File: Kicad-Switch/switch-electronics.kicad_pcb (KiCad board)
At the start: 2 copper layers, 99.1 x 99.1 mm, 95 parts, among them M1 CONN_1, P1 CONN_12, Q1 2N3906, Q10 SQD45P03-12-GE3, Q12 SQD45P03-12-GE3, Q13 SQD45P03-12-GE3, Q15 SQD45P03-12-GE3, Q16 SQD45P03-12-GE3, Q18 SQD45P03-12-GE3, Q2 2N3906, Q3 2N3906, Q4 2N3906, Q5 2N3906, Q6 2N3906, Q7 2N3906, Q8 2N3906, Q9 2N3906, U1 74HC04, U2 74LS139, U3 74HC04, U4 74LS139, U7 LM7809CT, U8 LM1084IT-3.3/NOPB

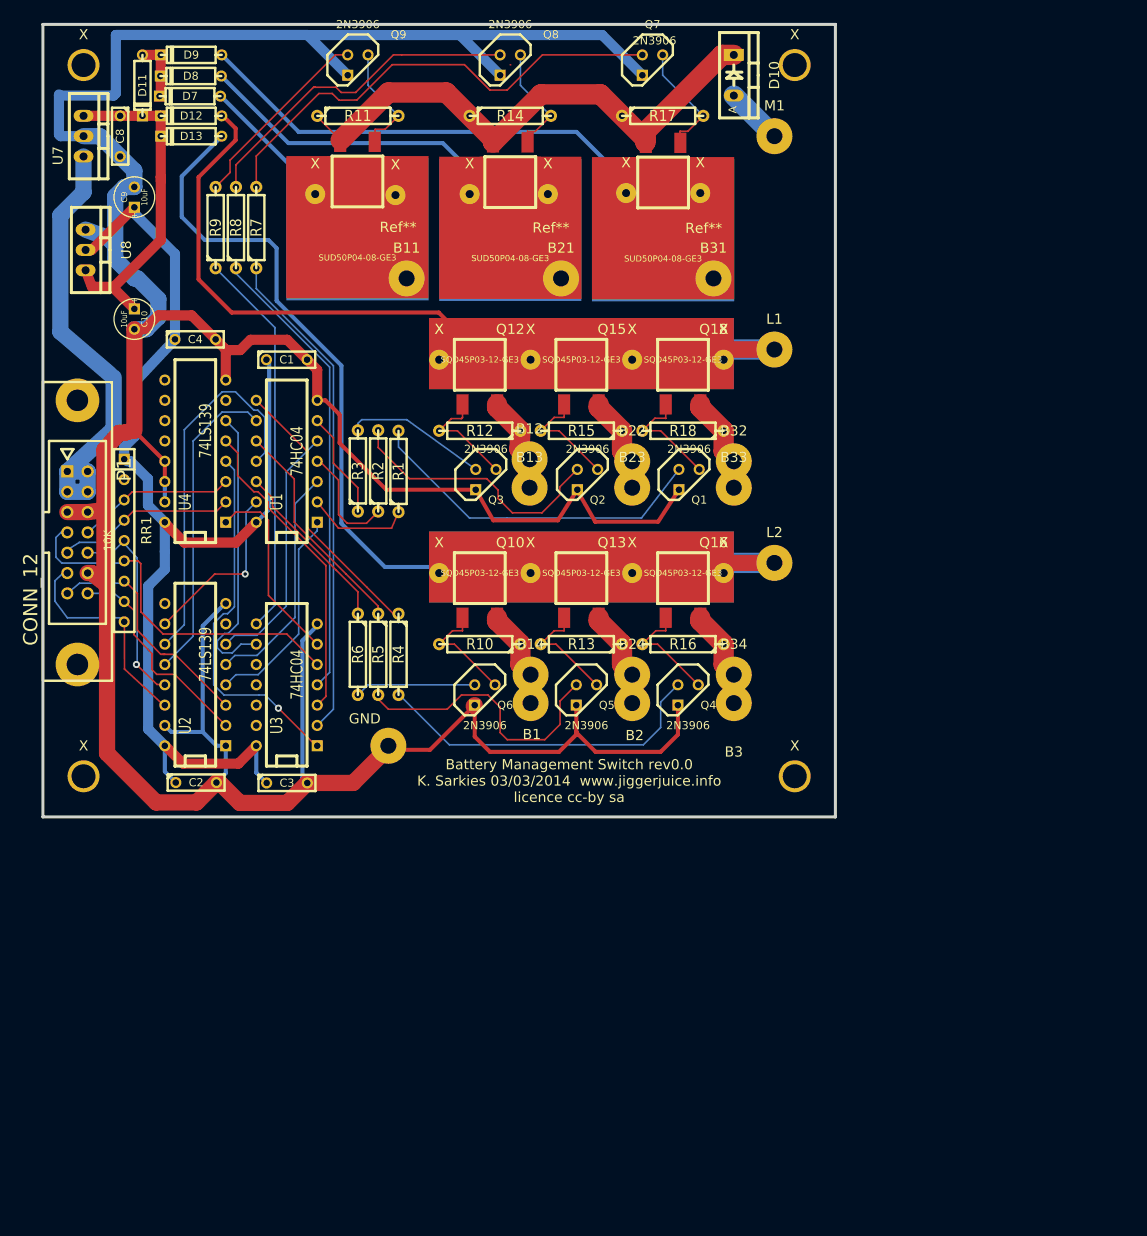
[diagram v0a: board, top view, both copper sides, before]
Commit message: Switch PCB: first Kicad version complete, not yet verified.
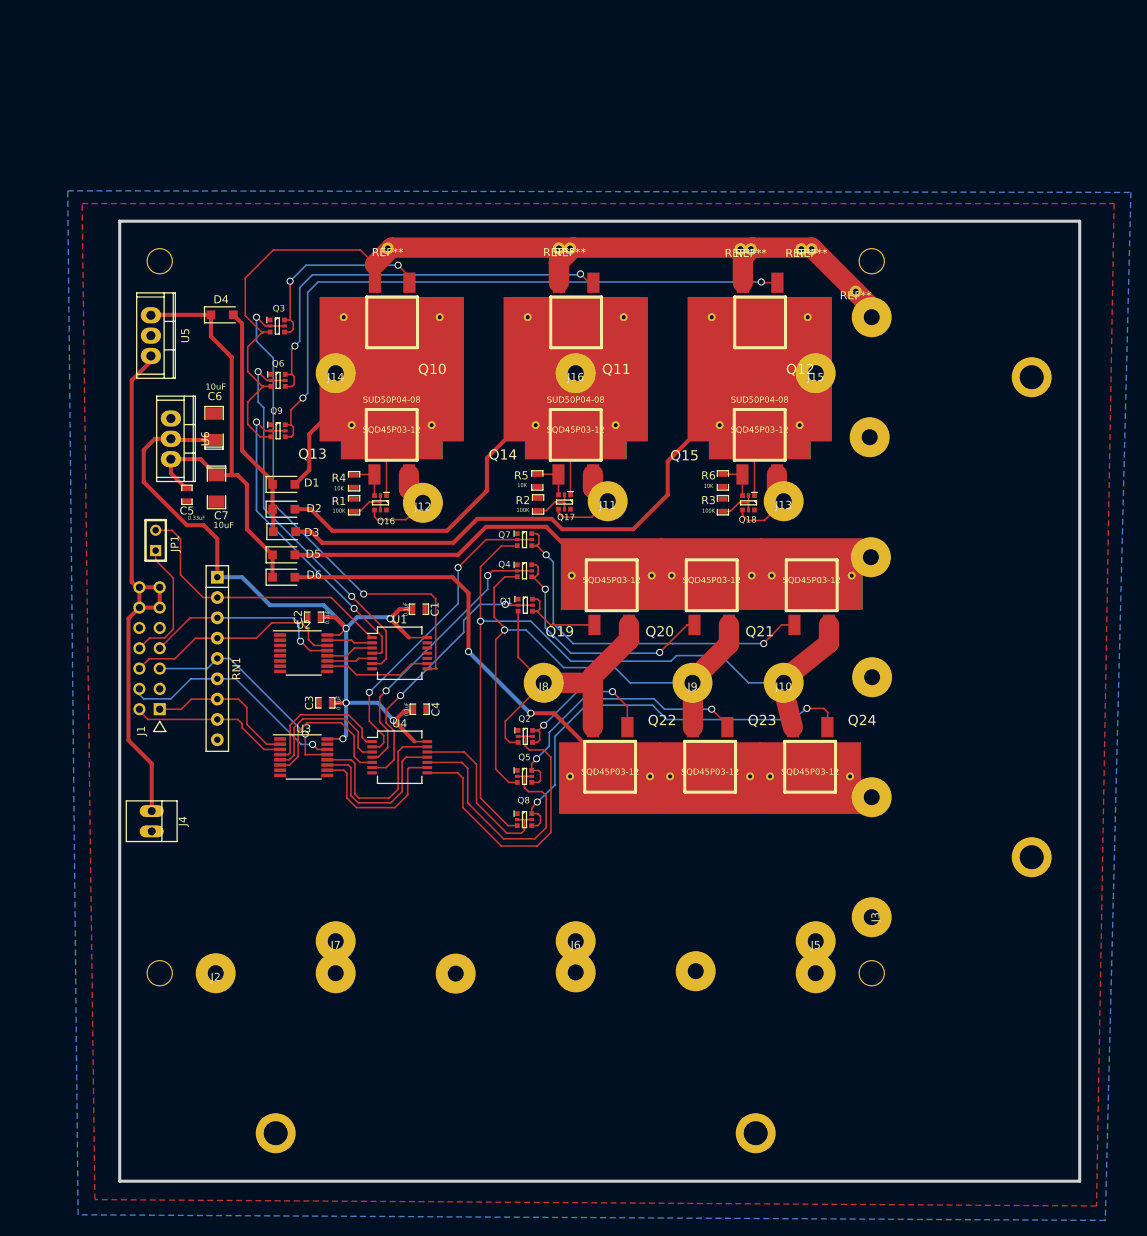
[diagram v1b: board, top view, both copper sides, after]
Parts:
- removed B1, B11, B12, B13, B14, B2, B21, B22, B23, B24, B3, B31, B32, B33, B34, GND, L1, L2, M1: CONN_1, SolderWirePad_single_2mmDrill
- removed C10, C9: 10uF, C1V5
- removed C8: 0.1uF, C2
- removed D10: MBR1645, Diode_TO-220_Vertical
- removed D11, D7, D8, D9: 1N4701, D3
- removed D12, D13: 1N5819, D3
- removed P1: CONN_12, he10-14d
- removed R10, R11, R12, R13, R14, R15, R16, R17, R18: 1K, R4
- removed R7, R8, R9: 10K, R4
- removed RR1: 10K, r_pack8
- removed Ref** (x3): SUD50P04-08-GE3, Fred:TO252-HS
- removed U7: LM7809CT, TO-220_Neutral123_Vertical
- removed U8: LM1084IT-3.3/NOPB, Transistors_TO-220:TO-220_Neutral123_Vertical
- removed X (x4): SolderWirePad_single_2mmDrill, SolderWirePad_single_2mmDrill
- removed X (x14): SolderWirePad_single_1mmDrill, SolderWirePad_single_1mmDrill
- added ?: MountingHole, BMS:Mounting_Hole_3mm, F.Cu at (40.0, 55.0)
- added ?: MountingHole, BMS:Mounting_Hole_3mm, F.Cu at (129.0, 55.0)
- added ?: MountingHole, BMS:Mounting_Hole_3mm, F.Cu at (129.0, 144.0)
- added ?: MountingHole, BMS:Mounting_Hole_3mm, F.Cu at (40.0, 144.0)
- added C5: 0.33uF, BMS:SM0603_Capa, F.Cu at (43.4, 84.2)
- added C6: 10uF, BMS:SM1206POL, F.Cu at (46.8, 75.7)
- added C7: 10uF, BMS:SM1206POL, F.Cu at (47.1, 83.4)
- added D1: 1N4001, BMS:D_SOD-123F, F.Cu at (55.5, 82.9)
- added D2: 1N4001, BMS:D_SOD-123F, F.Cu at (55.5, 86.0)
- added D3: 1N4001, BMS:D_SOD-123F, F.Cu at (55.6, 88.8)
- added D4: 1N4001, BMS:D_SOD-123F, F.Cu at (47.8, 61.7)
- added D5: 2N5819, BMS:D_SOD-123F, F.Cu at (55.5, 91.7)
- added D6: 2N5819, BMS:D_SOD-123F, F.Cu at (55.5, 94.5)
- added J1: Conn_02x07_Odd_Even, BMS:header-14-v, F.Cu at (40.0, 111.0)
- added J10: Conn_01x01, BMS:Pad_Large, F.Cu at (118.0, 107.7)
- added J11: Conn_01x01, BMS:Pad_Large, F.Cu at (96.0, 85.0)
- added J12: Conn_01x01, BMS:Pad_Large, F.Cu at (72.9, 85.2)
- added J13: Conn_01x01, BMS:Pad_Large, F.Cu at (118.0, 85.0)
- added J14: Conn_01x01, BMS:Pad_Large, F.Cu at (62.0, 69.0)
- added J15: Conn_01x01, BMS:Pad_Large, F.Cu at (122.0, 69.0)
- added J16: Conn_01x01, BMS:Pad_Large, F.Cu at (92.0, 69.0)
- added J2: Screw_Terminal_01x06, BMS:Screw_Terminal_Six, F.Cu at (47.0, 144.0)
- added J3: Screw_Terminal_01x06, BMS:Screw_Terminal_Six, F.Cu at (129.0, 137.0)
- added J4: Conn_01x02, BMS:PINHEAD1-2, F.Cu at (39.0, 125.0)
- added J5: Conn_01x01, BMS:Pad_Large, F.Cu at (122.0, 140.0)
- added J6: Conn_01x01, BMS:Pad_Large, F.Cu at (92.0, 140.0)
- added J7: Conn_01x01, BMS:Pad_Large, F.Cu at (62.0, 140.0)
- added J8: Conn_01x01, BMS:Pad_Large, F.Cu at (88.0, 107.7)
- added J9: Conn_01x01, BMS:Pad_Large, F.Cu at (106.6, 107.7)
- added JP1: Jumper_NO_Small, BMS:SIL-2, F.Cu at (39.5, 89.9)
- added Q11: SUD50P04-08, BMS:TO252-HS-Large, F.Cu at (92.0, 52.0)
- added Q14: SQD45P03-12, BMS:TO252-HS-Small, F.Cu at (92.0, 87.5)
- added Q17: BC856BDW1, BMS:SOT-363, F.Cu at (90.6, 85.1)
- added Q19: SQD45P03-12, BMS:TO252-HS-Small, F.Cu at (96.5, 106.3)
- added Q20: SQD45P03-12, BMS:TO252-HS-Small, F.Cu at (109.0, 106.3)
- added Q21: SQD45P03-12, BMS:TO252-HS-Small, F.Cu at (121.5, 106.3)
- added Q22: SQD45P03-12, BMS:TO252-HS-Small, F.Cu at (96.3, 107.4)
- added Q23: SQD45P03-12, BMS:TO252-HS-Small, F.Cu at (108.8, 107.4)
- added Q24: SQD45P03-12, BMS:TO252-HS-Small, F.Cu at (121.3, 107.4)
- added REF**: , BMS:Pad_Small, F.Cu at (127.0, 58.8)
- added REF**: , BMS:Pad_Small, F.Cu at (121.5, 53.5)
- added REF**: , BMS:Pad_Small, F.Cu at (120.2, 53.5)
- added REF**: , BMS:Pad_Small, F.Cu at (113.9, 53.5)
- added REF**: , BMS:Pad_Small, F.Cu at (112.6, 53.5)
- added REF**: , BMS:Pad_Small, F.Cu at (91.3, 53.4)
- added REF**: , BMS:Pad_Small, F.Cu at (89.9, 53.4)
- added REF**: , BMS:Pad_Small, F.Cu at (68.5, 53.4)
- added RN1: R_Network08, BMS:R_Array_SIP9, F.Cu at (47.2, 94.5)
- added U5: LM7809_TO220, BMS:TO-220, F.Cu at (38.9, 64.3)
- added U6: LM1086-3.3, BMS:TO-220, F.Cu at (41.4, 77.2)
- C1, C2, C3, C4: footprint C2 -> BMS:SM0603_Capa
- Q1, Q2, Q3, Q4, Q5, Q6, Q7, Q8, Q9: value 2N3906 -> BC847BPDW1; footprint TO92-CBE -> BMS:SOT-363
- Q10, Q12: value SQD45P03-12-GE3 -> SUD50P04-08; footprint TO252-HS-S -> BMS:TO252-HS-Large
- Q13, Q15: value SQD45P03-12-GE3 -> SQD45P03-12; footprint TO252-HS-S -> BMS:TO252-HS-Small
- Q16, Q18: value SQD45P03-12-GE3 -> BC856BDW1; footprint TO252-HS-S -> BMS:SOT-363
- R1, R2, R3: value 10K -> 100K; footprint R4 -> BMS:SM0603_Resistor
- R4, R5, R6: footprint R4 -> BMS:SM0603_Resistor
- U1: footprint DIP-14__300 -> BMS:SSOP-14
- U2: footprint DIP-16__300 -> BMS:TSSOP-16
- U3: value 74HC04 -> 74LS139; footprint DIP-14__300 -> BMS:TSSOP-16
- U4: value 74LS139 -> 74HC04; footprint DIP-16__300 -> BMS:SSOP-14
- moved Q8 94.3 mm to (85.6, 124.8)
- moved Q7 61.4 mm to (85.6, 89.8)
- moved Q10 54.5 mm to (69.0, 52.0), turned to 180 degrees
- moved C4 54.1 mm to (72.5, 111.0)
- moved R6 50.5 mm to (110.4, 82.4)
- moved Q6 47.1 mm to (54.8, 69.9)
- moved Q9 46.8 mm to (54.8, 76.2)
- moved U4 46.0 mm to (70.0, 117.0), turned to 0 degrees
- moved R3 45.8 mm to (110.4, 85.5)
- moved Q12 44.0 mm to (115.0, 52.0), turned to 180 degrees
- moved Q16 42.9 mm to (67.6, 85.2), turned to 270 degrees
- moved C1 35.3 mm to (72.4, 98.5)
- moved Q2 33.0 mm to (85.7, 114.4)
- moved Q3 32.4 mm to (54.7, 63.1)
- moved Q13 29.7 mm to (69.0, 87.5)
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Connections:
- R1 pad 1: Net-(R1-Pad1) -> Net-(Q16-Pad2)
- R1 pad 2: Net-(Q1-PadB) -> GND
- R2 pad 1: Net-(R2-Pad1) -> Net-(Q17-Pad2)
- R2 pad 2: Net-(Q2-PadB) -> GND
- R3 pad 1: Net-(R3-Pad1) -> Net-(Q18-Pad2)
- R3 pad 2: Net-(Q3-PadB) -> GND
- R4 pad 1: Net-(R4-Pad1) -> Net-(Q13-Pad1)
- R4 pad 2: Net-(Q4-PadB) -> GND
- R5 pad 1: Net-(R5-Pad1) -> Net-(Q14-Pad1)
- R5 pad 2: Net-(Q5-PadB) -> GND
- R6 pad 1: Net-(R6-Pad1) -> Net-(Q15-Pad1)
- R6 pad 2: Net-(Q6-PadB) -> GND
- U1 pad 1: Net-(U1-Pad1) -> Net-(JP1-Pad2)
- U1 pad 10: Net-(R5-Pad1) -> Net-(U1-Pad10)
- U1 pad 11: Net-(U1-Pad11) -> GND
- U1 pad 12: Net-(R6-Pad1) -> Net-(U1-Pad12)
- U1 pad 13: Net-(U1-Pad13) -> GND
- U1 pad 2: Net-(R1-Pad1) -> Net-(U1-Pad2)
- U1 pad 4: Net-(R2-Pad1) -> Net-(Q9-Pad2)
- U1 pad 6: Net-(R3-Pad1) -> Net-(Q6-Pad2)
- U1 pad 8: Net-(R4-Pad1) -> Net-(Q3-Pad2)
- U2 pad 10: Net-(U1-Pad13) -> Net-(U1-Pad9)
- U2 pad 11: Net-(U1-Pad11) -> Net-(U1-Pad5)
- U2 pad 12: Net-(U1-Pad9) -> Net-(U1-Pad3)
- U2 pad 13: L2.0 -> Net-(J1-Pad7)
- U2 pad 14: L2.1 -> Net-(J1-Pad6)
- U2 pad 15: GND -> Net-(U1-Pad2)
- U2 pad 2: L1.1 -> GND
- U2 pad 3: L1.0 -> GND
- U2 pad 4: Net-(U1-Pad1) -> Net-(U2-Pad4)
- U2 pad 5: Net-(U1-Pad3) -> Net-(U2-Pad5)
- U2 pad 6: Net-(U1-Pad5) -> Net-(U2-Pad6)
- U3 pad 1: Net-(U3-Pad1) -> GND
- U3 pad 10: (no net) -> Net-(U3-Pad10)
- U3 pad 11: (no net) -> Net-(U3-Pad11)
- U3 pad 12: (no net) -> Net-(U3-Pad12)
- U3 pad 13: (no net) -> Net-(J1-Pad5)
- U3 pad 14: VCC -> Net-(J1-Pad4)
- U3 pad 3: Net-(U3-Pad3) -> Net-(J1-Pad2)
- U3 pad 4: Net-(R8-Pad1) -> Net-(U3-Pad4)
- U3 pad 5: PWM -> Net-(U3-Pad5)
- U3 pad 7: GND -> Net-(U3-Pad7)
- U3 pad 8: Net-(R9-Pad1) -> GND
- U4 pad 1: Net-(U3-Pad6) -> Net-(U3-Pad4)
- U4 pad 10: Net-(U4-Pad10) -> Net-(Q5-Pad2)
- U4 pad 11: Net-(U4-Pad11) -> Net-(U3-Pad11)
- U4 pad 12: Net-(U4-Pad12) -> Net-(Q8-Pad2)
- U4 pad 13: GND -> Net-(U3-Pad12)
- U4 pad 14: GND -> VCC
- U4 pad 2: M1.1 -> Net-(Q7-Pad2)
- U4 pad 3: M1.0 -> Net-(U3-Pad5)
- U4 pad 4: Net-(U3-Pad1) -> Net-(Q4-Pad2)
- U4 pad 5: Net-(U3-Pad3) -> Net-(U3-Pad6)
- U4 pad 6: Net-(U3-Pad9) -> Net-(Q1-Pad2)
- U4 pad 7: Net-(U4-Pad7) -> GND
- U4 pad 8: GND -> Net-(Q2-Pad2)
- U4 pad 9: Net-(U4-Pad9) -> Net-(U3-Pad10)
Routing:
- net GND: track 409.6 -> 0.00 mm
- net M1: track 0.00 -> 125.3 mm
- net B3: track 0.00 -> 108.9 mm, vias 0 -> 1
- net Net-(D3-Pad2): track 0.00 -> 99.3 mm
- net B2: track 0.00 -> 83.5 mm, vias 0 -> 1
- net Net-(D13-Pad1): track 83.0 -> 0.00 mm
- net Net-(D2-Pad2): track 0.00 -> 74.6 mm
- net Net-(D9-Pad1): track 72.1 -> 0.00 mm
- net Net-(D10-Pad2): track 69.2 -> 0.00 mm
- net B3M1: track 14.8 -> 79.9 mm, vias 0 -> 2
- net Net-(D6-Pad2): track 0.00 -> 63.4 mm, vias 0 -> 2
- net Net-(Q3-Pad2): track 0.00 -> 63.4 mm, vias 0 -> 2
- net Net-(D12-Pad1): track 62.2 -> 0.00 mm
- net Net-(Q7-PadB): track 60.7 -> 0.00 mm
- net L2.0: track 57.7 -> 0.00 mm, vias 1 -> 0
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- added copper zone on B.Cu, net GND
- added copper zone on F.Cu, net GND
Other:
- board size 99.1 x 99.1 mm -> 120 x 120 mm
- board text removed: "Battery Management Switch rev0.0 K. Sarkies 03/03/2014 www.jiggerjuice.info licence cc-by sa"

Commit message: Complete PCB apart from some points that Kicad doesn't consider to be connected. Reduce size to 100mmx100mm to reduce manufacturing costs.
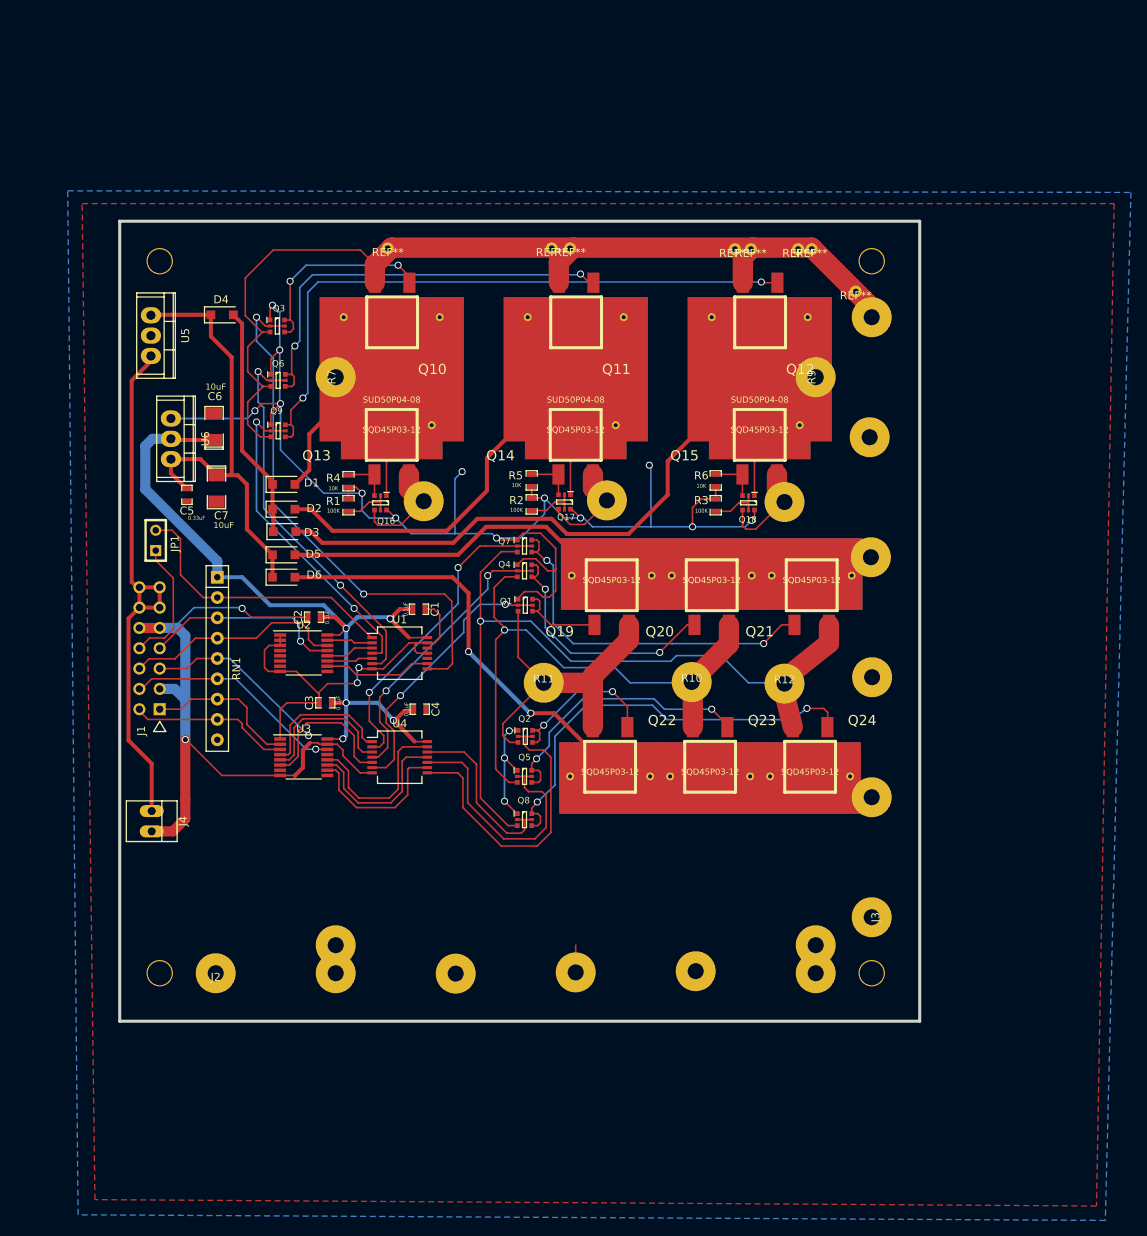
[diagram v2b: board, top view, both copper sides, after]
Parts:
- removed J10, J11, J12, J13, J14, J15, J16, J5, J6, J7, J8, J9: Conn_01x01, BMS:Pad_Large
- added R10: 0, BMS:Link_3, F.Cu at (106.5, 107.6)
- added R11: 0, BMS:Link_2, F.Cu at (88.0, 107.7)
- added R12: 0, BMS:Link_4, F.Cu at (118.1, 107.8)
- added R7: 0, BMS:Link_1, F.Cu at (62.0, 69.5)
- added R9: 0, BMS:Link_1, F.Cu at (122.0, 69.5)
- moved R3 0.90 mm to (109.5, 85.5)
- moved R6 0.90 mm to (109.5, 82.4)
- moved REF** 0.90 mm to (89.0, 53.4)
- moved Q7 0.80 mm to (85.6, 90.6)
- moved R2 0.80 mm to (86.5, 85.4)
- moved R5 0.70 mm to (86.5, 82.4)
- moved R1 0.70 mm to (63.6, 85.5)
- moved R4 0.70 mm to (63.6, 82.5)
- moved REF** 0.70 mm to (111.9, 53.5)
- moved REF** 0.40 mm to (119.8, 53.5)
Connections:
- J2 pad 2: Net-(D1-Pad2) -> Net-(J2-Pad2)
- J2 pad 4: Net-(D2-Pad2) -> Net-(J2-Pad4)
- J2 pad 6: Net-(D3-Pad2) -> Net-(J2-Pad6)
- Q13 pad 2: B1 -> Net-(Q13-Pad2)
- Q14 pad 2: B2 -> Net-(Q14-Pad2)
- Q15 pad 2: B3 -> Net-(Q15-Pad2)
- Q16 pad 4: B1 -> Net-(Q13-Pad2)
- Q17 pad 4: B2 -> Net-(Q14-Pad2)
- Q18 pad 4: B3 -> Net-(Q15-Pad2)
- REF** pad 1: (no net) -> M1 (x8)
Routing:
- net GND: track 0.00 -> 324.2 mm, vias 0 -> 20
- net Net-(Q13-Pad2): track 0.00 -> 13.1 mm
- net Net-(Q15-Pad2): track 0.00 -> 12.4 mm
- net Net-(Q14-Pad2): track 0.00 -> 12.4 mm
- net B1: track 54.4 -> 42.5 mm
- net B2: track 83.5 -> 71.8 mm
- net Net-(D3-Pad2): track 99.3 -> 87.7 mm
- net Net-(D2-Pad2): track 74.6 -> 63.0 mm
- net B3: track 108.9 -> 97.5 mm
- net Net-(D1-Pad2): track 36.8 -> 43.6 mm
- net Net-(J1-Pad5): track 28.0 -> 23.1 mm
- net Net-(J2-Pad6): track 0.00 -> 3.50 mm
- net Net-(J2-Pad2): track 0.00 -> 3.50 mm
- net Net-(J2-Pad4): track 0.00 -> 3.40 mm
- net Net-(Q3-Pad2): track 63.4 -> 66.7 mm
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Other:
- board size 120 x 120 mm -> 100 x 100 mm
- net class Default: clearance 0.254 -> 0.2
- rule trace_clearance: 0.254 -> 0.2

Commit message: Managed to convince Kicad to agree that certain nets were connected to their pads, after adding multiple overlay tracks. Now DRC error free. Adjusted tracks and grounds to ensure that most blank areas were covered with a ground plane. Added Text and OSHW logo.
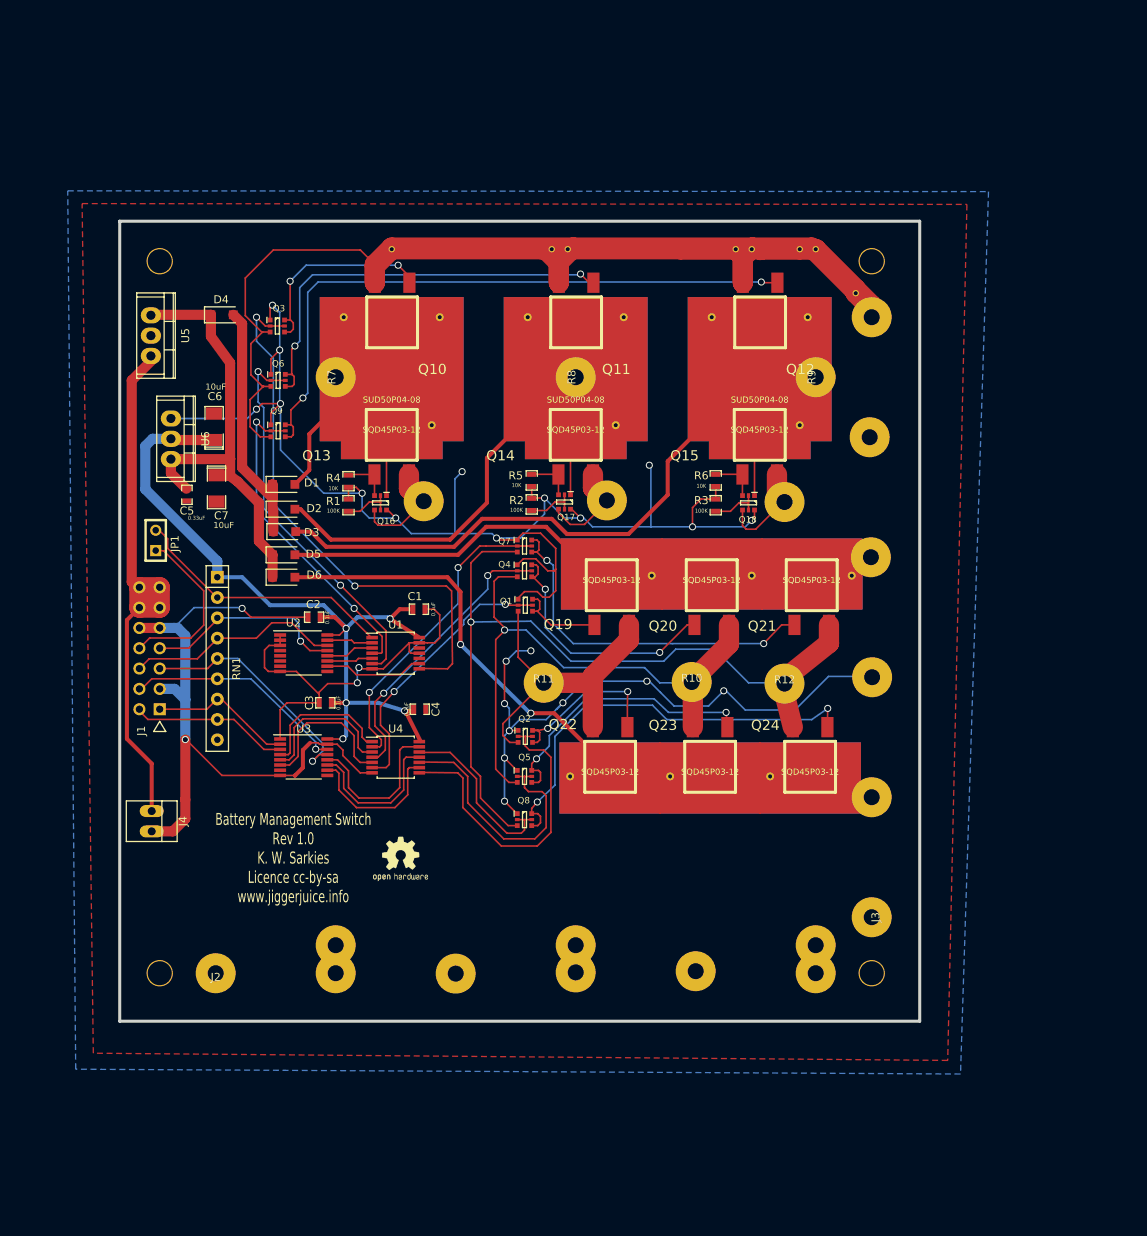
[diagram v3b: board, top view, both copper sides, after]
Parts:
- removed REF** (x8): , BMS:Pad_Small
- added G***: LOGO, OPENHARDWARE:OSHWLOGO0.3IN, F.Cu at (66.3, 126.0)
- added J10: Conn_01x01, BMS:THROUGHVIA, F.Cu at (89.0, 53.5)
- added J11: Conn_01x01, BMS:THROUGHVIA, F.Cu at (127.0, 59.0)
- added J12: Conn_01x01, BMS:THROUGHVIA, F.Cu at (112.0, 53.5)
- added J5: Conn_01x01, BMS:THROUGHVIA, F.Cu at (69.0, 53.5)
- added J6: Conn_01x01, BMS:THROUGHVIA, F.Cu at (91.0, 53.5)
- added J7: Conn_01x01, BMS:THROUGHVIA, F.Cu at (114.0, 53.5)
- added J8: Conn_01x01, BMS:THROUGHVIA, F.Cu at (120.0, 53.5)
- added J9: Conn_01x01, BMS:THROUGHVIA, F.Cu at (122.0, 53.5)
- added R8: 0, BMS:Link_1, F.Cu at (92.0, 69.5)
- U1, U4: footprint BMS:SSOP-14 -> BMS:TSSOP-14
- moved U1 0.50 mm to (69.5, 104.0)
- moved U4 0.50 mm to (69.5, 117.0)
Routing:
- net M1: track 125.1 -> 258.6 mm
- net GND: track 324.2 -> 390.4 mm, vias 20 -> 26
- net Net-(D5-Pad2): track 51.8 -> 76.8 mm
- net Net-(D6-Pad2): track 63.4 -> 88.0 mm
- net Net-(J1-Pad5): track 23.1 -> 30.3 mm
- net Net-(J1-Pad8): track 16.0 -> 21.6 mm
- net B3: track 97.5 -> 101.8 mm
- net Net-(D1-Pad1): track 29.2 -> 32.6 mm
- net VCC: track 102.5 -> 99.2 mm
- net Net-(JP1-Pad2): track 35.2 -> 33.3 mm
- net Net-(Q3-Pad2): track 66.7 -> 68.5 mm
- net Net-(D2-Pad2): track 63.0 -> 64.7 mm
- net Net-(J1-Pad1): track 19.1 -> 17.9 mm
- net B1L2: track 20.2 -> 21.2 mm
- net Net-(U3-Pad12): track 21.1 -> 20.2 mm
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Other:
- board text added: "Battery Management Switch Rev 1.0 K. W. Sarkies Licence cc-by-sa www.jiggerjuice.info"
